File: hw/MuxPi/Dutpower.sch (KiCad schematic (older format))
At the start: 23 parts, among them P2 XY2500V-D(5.08)-2PIN, P3 XY2500V-D(5.08)-2PIN, Q1 2N7002, U15 MCP6002-E/SN, U4 ACS712ELCTR-05B-T

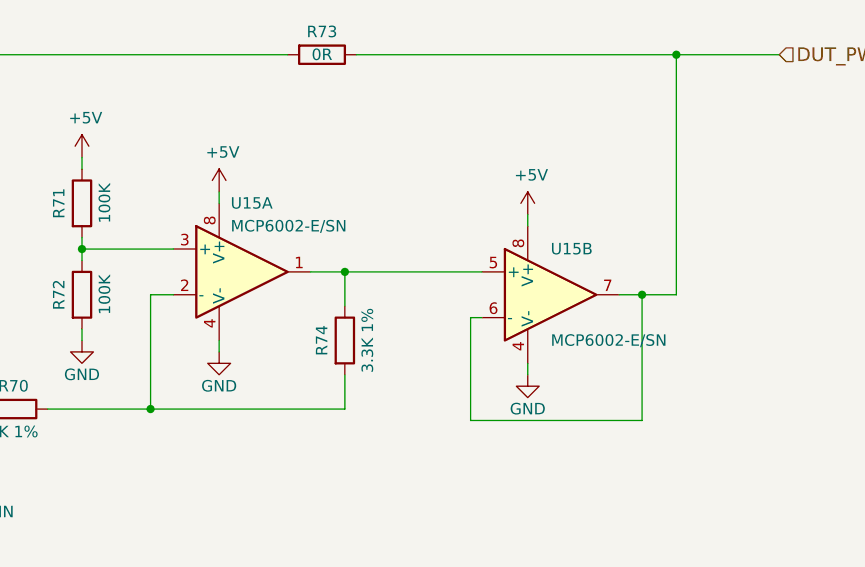
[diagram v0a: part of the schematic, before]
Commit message: Add detailed info to MuxPi electronic components
The additional information includes manufacturer names and
manufacturer symbols for all components except ceramic capacitors
and resistors. It allows to create BOM (Bill Of Materials) with
actual product names.

Change-Id: Id1c518bba60322d4b8b132ad14261806070abc27
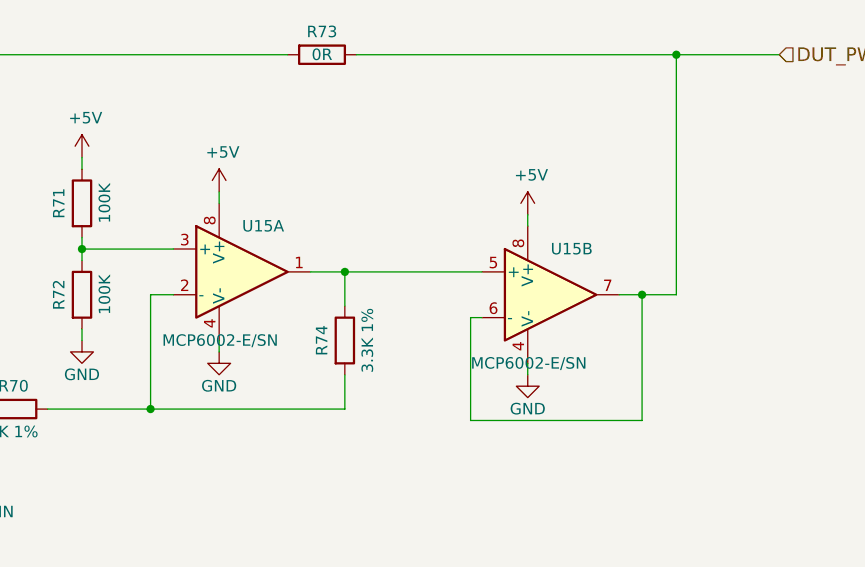
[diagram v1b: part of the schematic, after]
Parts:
- D1: Manufacturer (none) -> TAIWAN SEMICONDUCTOR; Symbol (none) -> ES1JL
- D12: Manufacturer (none) -> ON SEMICONDUCTOR (FAIRCHILD); Symbol (none) -> 1N4448WS
- P2, P3: Complementary manufacturer (none) -> XINYA; Complementary symbol (none) -> XY2500F-BV(5.08)-2P; Manufacturer (none) -> XINYA; Symbol (none) -> XY2500V-D(5.08)-2PIN
- Q1: Manufacturer (none) -> ON SEMICONDUCTOR (FAIRCHILD); Symbol (none) -> 2N7002
- RL1: Manufacturer (none) -> FUJITSU-TAKAMISAWA; Symbol (none) -> JV-5S-KT
- U15: Manufacturer (none) -> MICROCHIP TECHNOLOGY; Symbol (none) -> MCP6002-E/SN
- U4: Manufacturer (none) -> ALLEGRO MICROSYSTEMS; Symbol (none) -> ACS712ELCTR-05B-T
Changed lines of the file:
@@
 F 3 "http://www.tme.eu/pl/Document/6e3ed172b8ef57eec12ad172948b8283/ES1JL-DTE.pdf" H 3900 5000 60  0001 C CNN
 F 4 "http://www.tme.eu/pl/details/es1jl/diody-uniwersalne-smd/taiwan-semiconductor/" H 3900 5000 60  0001 C CNN "Shop link"
+F 5 "TAIWAN SEMICONDUCTOR" H 3900 5000 50  0001 C CNN "Manufacturer"
+F 6 "ES1JL" H 3900 5000 50  0001 C CNN "Symbol"
 	1    3900 5000
 	1    0    0    -1
@@
 F 3 "http://www.tme.eu/pl/Document/160416a7d37511bbe210dab3bc04735d/jv.pdf" H 3900 4400 50  0001 C CNN
 F 4 "http://www.tme.eu/pl/details/jv-5s-kt/przekazniki-elektromagn-miniaturowe/fujitsu-takamisawa/" V 3900 4400 60  0001 C CNN "Shop link"
+F 5 "FUJITSU-TAKAMISAWA" V 3900 4400 50  0001 C CNN "Manufacturer"
+F 6 "JV-5S-KT" V 3900 4400 50  0001 C CNN "Symbol"
 	1    3900 4400
 	0    -1   -1   0
@@
 F 4 "http://www.tme.eu/pl/details/tbg-5-pw-2p-gn/listwy-zaciskowe-do-druku/xinya/xy2500v-d508-2pin/" H 2300 3900 60  0001 C CNN "Shop link"
 F 5 "http://www.tme.eu/pl/details/tbw-5.08-2p/listwy-zaciskowe-do-druku/xinya/xy2500f-bv508-2p/" H 2300 3900 60  0001 C CNN "Complementary device"
+F 6 "XINYA" H 2300 3900 50  0001 C CNN "Complementary manufacturer"
+F 7 "XY2500F-BV(5.08)-2P" H 2300 3900 50  0001 C CNN "Complementary symbol"
+F 8 "XINYA" H 2300 3900 50  0001 C CNN "Manufacturer"
+F 9 "XY2500V-D(5.08)-2PIN" H 2300 3900 50  0001 C CNN "Symbol"
 	1    2300 3900
 	-1   0    0    -1
@@
 F 3 "http://www.farnell.com/datasheets/64754.pdf?_ga=1.192000233.291132730.1474618953" H 1690 1690 60  0001 C CNN
 F 4 "http://pl.farnell.com/allegro-microsystems/acs712elctr-05b-t/ic-sensor-current-5a-soic8/dp/1329623" V 3900 2800 60  0001 C CNN "Shop link"
+F 5 "ALLEGRO MICROSYSTEMS" V 3900 2800 50  0001 C CNN "Manufacturer"
+F 6 "ACS712ELCTR-05B-T " V 3900 2800 50  0001 C CNN "Symbol"
 	1    3900 2800
 	0    -1   -1   0
@@
 	0    1    1    0
 $EndComp
-$Comp
-L MuxPi:2N7002 Q1
-U 1 1 584F2EFF
-P 4200 5300
-F 0 "Q1" H 4391 5346 50  0000 L CNN
-F 1 "2N7002" H 4391 5255 50  0000 L CNN
-F 2 "TO_SOT_Packages_SMD:SOT-23" H 4400 5225 50  0001 L CIN
-F 3 "https://www.nxp.com/documents/data_sheet/2N7002.pdf" H 4200 5300 50  0001 L CNN
-F 4 "http://www.tme.eu/pl/details/2n7002/tranzystory-z-kanalem-n-smd/fairchild-semiconductor/" H 4200 5300 60  0001 C CNN "Shop link"
-	1    4200 5300
-	1    0    0    -1
-$EndComp
-$Comp
-L MuxPi:CONN_01X02 P3
-U 1 1 584FF008
-P 5950 3900
-F 0 "P3" H 6028 3941 50  0000 L CNN
-F 1 "XY2500V-D(5.08)-2PIN" H 6028 3850 50  0000 L CNN
-F 2 "mux-footprints:TerminalBlock_XY2500V-D(5.08)" H 5950 3900 50  0001 C CNN
-F 3 "http://www.cresttech.com.au/pdf/Pluggable_connector.pdf" H 5950 3900 50  0001 C CNN
-F 4 "http://www.tme.eu/pl/details/tbg-5-pw-2p-gn/listwy-zaciskowe-do-druku/xinya/xy2500v-d508-2pin/" H 5950 3900 60  0001 C CNN "Shop link"
-F 5 "http://www.tme.eu/pl/details/tbw-5.08-2p/listwy-zaciskowe-do-druku/xinya/xy2500f-bv508-2p/" H 5950 3900 60  0001 C CNN "Complementary device"
-	1    5950 3900
-	1    0    0    -1
-$EndComp
 Wire Wire Line
 	4600 3950 5050 3950
@@
 F 3 "https://www.tme.eu/pl/Document/092852c2250de492ce82b1b9e9d241c4/1N4148WS.pdf" H 5750 1950 50  0001 C CNN
 F 4 "https://www.tme.eu/pl/details/1n4448ws/diody-uniwersalne-smd/on-semiconductor-fairchild/" H 5750 1950 50  0001 C CNN "Shop link"
+F 5 "ON SEMICONDUCTOR (FAIRCHILD)" H 5750 1950 50  0001 C CNN "Manufacturer"
+F 6 "1N4448WS" H 5750 1950 50  0001 C CNN "Symbol"
 	1    5750 1950
 	-1   0    0    1
@@
 Wire Wire Line
 	5450 1950 5600 1950
-$Comp
-L MuxPi:MCP6002 U15
-U 1 1 5A9F2BE3
-P 7800 2900
-F 0 "U15" H 7750 3200 50  0000 L CNN
-F 1 "MCP6002-E/SN" H 7750 3100 50  0000 L CNN
-F 2 "mux-footprints:SOIC-8" H 7700 2950 50  0001 C CNN
-F 3 "http://www.tme.eu/pl/Document/c98656c49a036767b89c9bb93e3dda4a/mcp6001_2_4.pdf" H 7800 3050 50  0001 C CNN
-F 4 "http://www.tme.eu/pl/details/mcp6002-e_sn/wzmacniacze-operacyjne-smd/microchip-technology/" H 7800 2900 60  0001 C CNN "Shop link"
-	1    7800 2900
-	1    0    0    -1
-$EndComp
-$Comp
-L MuxPi:MCP6002 U15
-U 2 1 5A9F2BEB
-P 9150 3000
-F 0 "U15" H 9150 3200 50  0000 L CNN
-F 1 "MCP6002-E/SN" H 9150 2800 50  0000 L CNN
-F 2 "mux-footprints:SOIC-8" H 9050 3050 50  0001 C CNN
-F 3 "http://www.tme.eu/pl/Document/c98656c49a036767b89c9bb93e3dda4a/mcp6001_2_4.pdf" H 9150 3150 50  0001 C CNN
-F 4 "http://www.tme.eu/pl/details/mcp6002-e_sn/wzmacniacze-operacyjne-smd/microchip-technology/" H 9150 3000 60  0001 C CNN "Shop link"
-	2    9150 3000
-	1    0    0    -1
-$EndComp
 $Comp
 L MuxPi:GND #PWR0215
@@
 Wire Wire Line
 	6400 1950 8000 1950
+$Comp
+L MuxPi:2N7002 Q1
+U 1 1 5A8B550D
+P 4200 5300
+F 0 "Q1" H 4391 5346 50  0000 L CNN
+F 1 "2N7002" H 4391 5255 50  0000 L CNN
+F 2 "TO_SOT_Packages_SMD:SOT-23" H 4400 5225 50  0001 L CIN
+F 3 "https://www.nxp.com/documents/data_sheet/2N7002.pdf" H 4200 5300 50  0001 L CNN
+F 4 "http://www.tme.eu/pl/details/2n7002/tranzystory-z-kanalem-n-smd/fairchild-semiconductor/" H 4200 5300 60  0001 C CNN "Shop link"
+F 5 "ON SEMICONDUCTOR (FAIRCHILD)" H 4200 5300 50  0001 C CNN "Manufacturer"
+F 6 "2N7002" H 4200 5300 50  0001 C CNN "Symbol"
+	1    4200 5300
+	1    0    0    -1
+$EndComp
+$Comp
+L MuxPi:CONN_01X02 P3
+U 1 1 5A8B8B5B
+P 5950 3900
+F 0 "P3" H 6028 3941 50  0000 L CNN
+F 1 "XY2500V-D(5.08)-2PIN" H 6028 3850 50  0000 L CNN
+F 2 "mux-footprints:TerminalBlock_XY2500V-D(5.08)" H 5950 3900 50  0001 C CNN
+F 3 "http://www.cresttech.com.au/pdf/Pluggable_connector.pdf" H 5950 3900 50  0001 C CNN
+F 4 "http://www.tme.eu/pl/details/tbg-5-pw-2p-gn/listwy-zaciskowe-do-druku/xinya/xy2500v-d508-2pin/" H 5950 3900 60  0001 C CNN "Shop link"
+F 5 "http://www.tme.eu/pl/details/tbw-5.08-2p/listwy-zaciskowe-do-druku/xinya/xy2500f-bv508-2p/" H 5950 3900 60  0001 C CNN "Complementary device"
+F 6 "XINYA" H 5950 3900 50  0001 C CNN "Complementary manufacturer"
+F 7 "XY2500F-BV(5.08)-2P" H 5950 3900 50  0001 C CNN "Complementary symbol"
+F 8 "XINYA" H 5950 3900 50  0001 C CNN "Manufacturer"
+F 9 "XY2500V-D(5.08)-2PIN" H 5950 3900 50  0001 C CNN "Symbol"
+	1    5950 3900
+	1    0    0    -1
+$EndComp
+$Comp
+L MuxPi:MCP6002 U15
+U 1 1 5A8BCDE3
+P 7800 2900
+F 0 "U15" H 7800 3100 50  0000 L CNN
+F 1 "MCP6002-E/SN" H 7450 2600 50  0000 L CNN
+F 2 "mux-footprints:SOIC-8" H 7700 2950 50  0001 C CNN
+F 3 "http://www.tme.eu/pl/Document/c98656c49a036767b89c9bb93e3dda4a/mcp6001_2_4.pdf" H 7800 3050 50  0001 C CNN
+F 4 "http://www.tme.eu/pl/details/mcp6002-e_sn/wzmacniacze-operacyjne-smd/microchip-technology/" H 7800 2900 60  0001 C CNN "Shop link"
+F 5 "MICROCHIP TECHNOLOGY" H 7800 2900 50  0001 C CNN "Manufacturer"
+F 6 "MCP6002-E/SN" H 7800 2900 50  0001 C CNN "Symbol"
+	1    7800 2900
+	1    0    0    -1
+$EndComp
+$Comp
+L MuxPi:MCP6002 U15
+U 2 1 5A8BF6A4
+P 9150 3000
+F 0 "U15" H 9150 3200 50  0000 L CNN
+F 1 "MCP6002-E/SN" H 8800 2700 50  0000 L CNN
+F 2 "mux-footprints:SOIC-8" H 9050 3050 50  0001 C CNN
+F 3 "http://www.tme.eu/pl/Document/c98656c49a036767b89c9bb93e3dda4a/mcp6001_2_4.pdf" H 9150 3150 50  0001 C CNN
+F 4 "http://www.tme.eu/pl/details/mcp6002-e_sn/wzmacniacze-operacyjne-smd/microchip-technology/" H 9150 3000 60  0001 C CNN "Shop link"
+F 5 "MICROCHIP TECHNOLOGY" H 9150 3000 50  0001 C CNN "Manufacturer"
+F 6 "MCP6002-E/SN" H 9150 3000 50  0001 C CNN "Symbol"
+	2    9150 3000
+	1    0    0    -1
+$EndComp
 $EndSCHEMATC

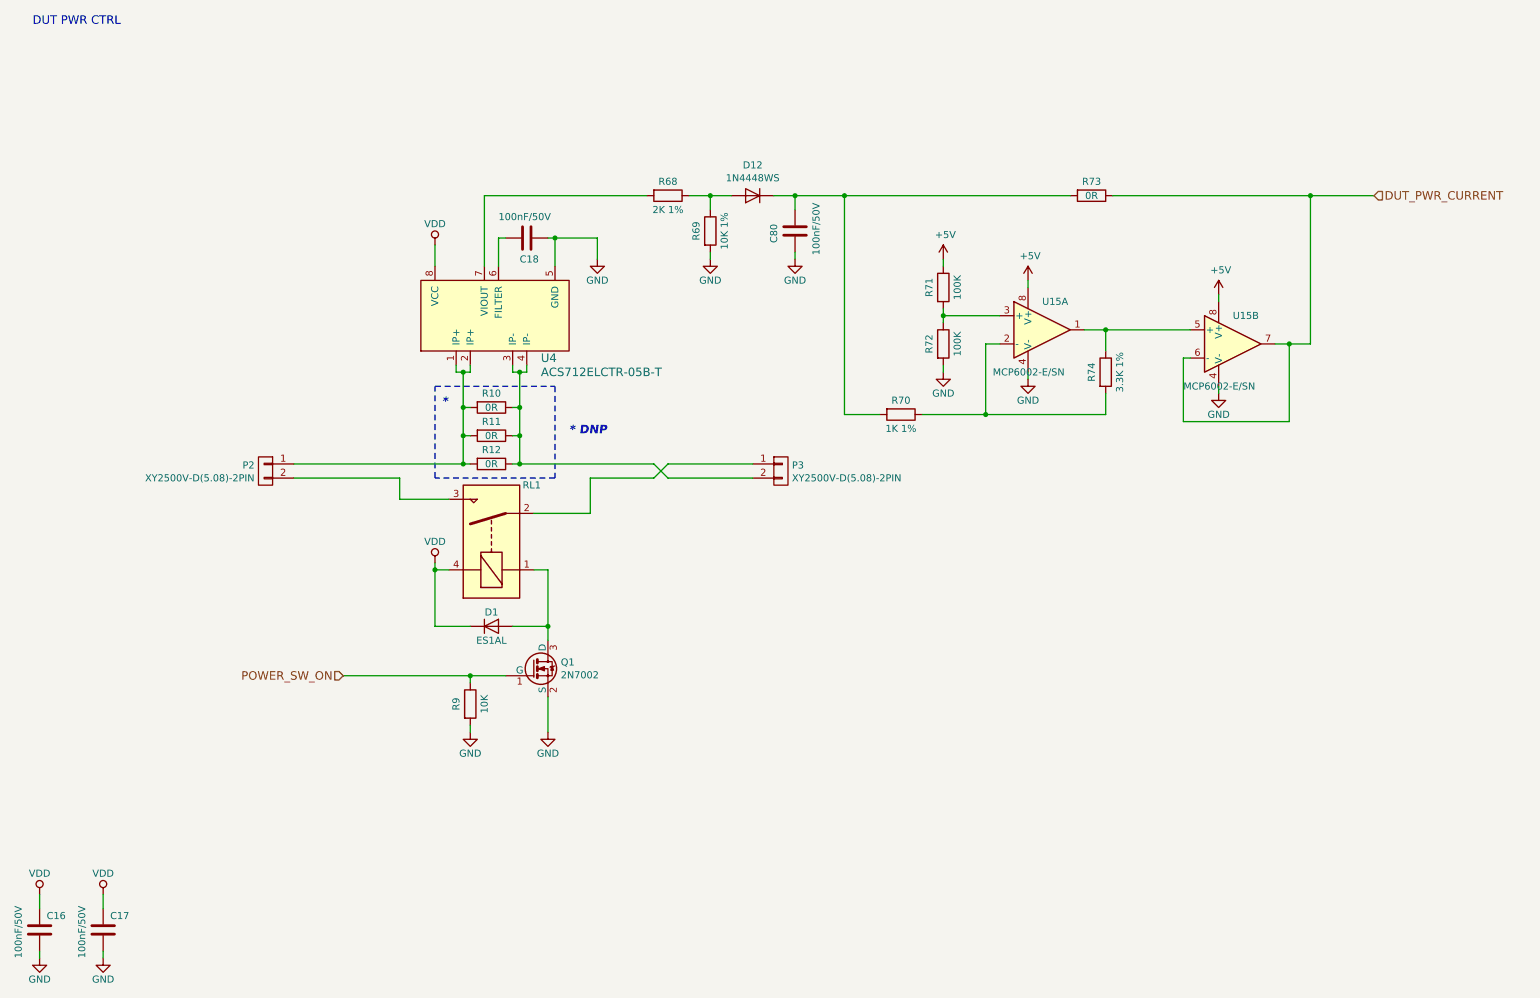
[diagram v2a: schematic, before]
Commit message: Update hardware design to version 1.2
Change-Id: I36445887bfaa5fada88d8bf3915603605de47512
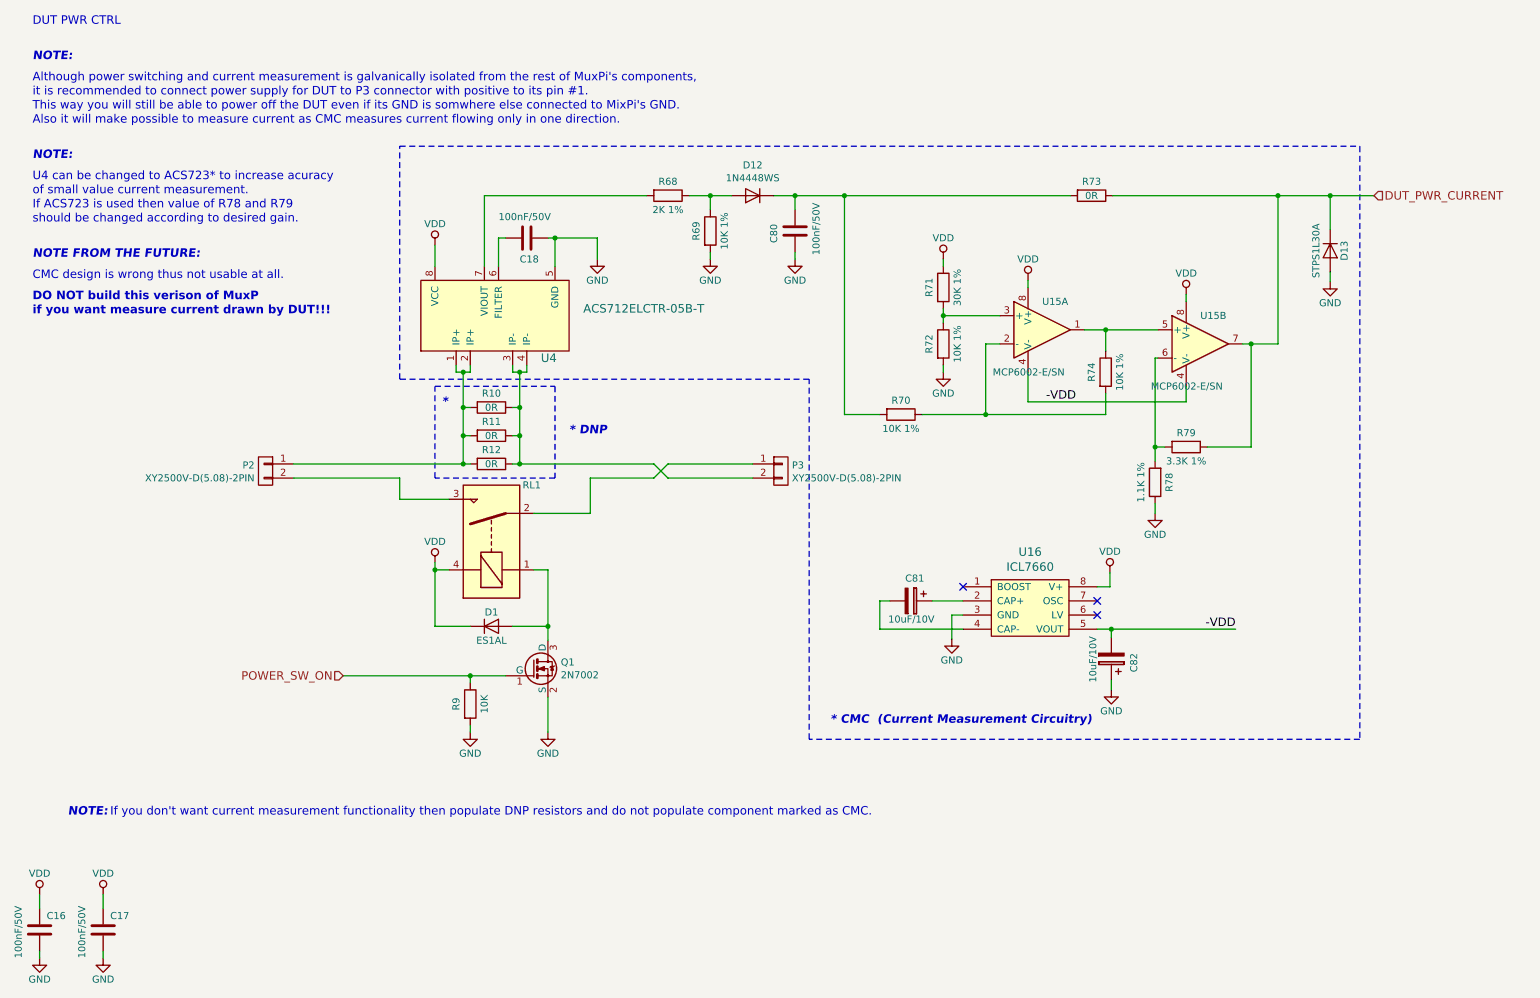
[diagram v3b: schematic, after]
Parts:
- added C81, C82: 10uF/10V, Capacitors_Tantalum_SMD:CP_Tantalum_Case-A_EIA-3216-18_Reflow, symbol MuxPi:CP
- added D13: STPS1L30A, mux-footprints:Sub_SMA, symbol MuxPi:D
- added R78: 1.1K 1%, Resistors_SMD:R_0805, symbol MuxPi:R
- added R79: 3.3K 1%, Resistors_SMD:R_0805, symbol MuxPi:R
- added U16: ICL7660, mux-footprints:SOIC-8, symbol MuxPi:ICL7660
- R70: value 1K 1% -> 10K 1%
- R71: value 100K -> 30K 1%
- R72: value 100K -> 10K 1%
- R74: value 3.3K 1% -> 10K 1%
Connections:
- net +5V is gone; now on net VDD: R71.1, U15.8 (V+), U15.8 (V+)
- net DUT_PWR_CURRENT: now also D13.1 (K), R79.1; no longer U15.6 (-)
- net GND: now also C82.1, D13.2 (A), R78.1, U16.3 (GND); no longer U15.4 (V-), U15.4 (V-)
- net VDD: now also U16.8 (V+)
- new net: R78.2, R79.2, U15.6 (-)
- new net: C81.1, U16.2 (CAP+)
- new net: C81.2, U16.4 (CAP-)
- new net -VDD: C82.2, U15.4 (V-), U15.4 (V-), U16.5 (VOUT)
- no-connect marks 0 -> 3
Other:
- note added: "* CMC (Current Measurement Circuitry)"
- note added: "Also it will make possible to measure current as CMC measures current flowing only in one direction."
- note added: "Although power switching and current measurement is galvanically isolated from the rest of MuxPi's components,"
- note added: "CMC design is wrong thus not usable at all.\n"
- note added: "DO NOT build this verison of MuxP"
- note added: "If ACS723 is used then value of R78 and R79"
- note added: "If you don't want current measurement functionality then populate DNP resistors and do not populate component marked as CMC."
- note added: "NOTE FROM THE FUTURE:\n"
- note added: "NOTE:"
- note added: "This way you will still be able to power off the DUT even if its GND is somwhere else connected to MixPi's GND."
- note added: "U4 can be changed to ACS723* to increase acuracy"
- note added: "if you want measure current drawn by DUT!!!"
- note added: "it is recommended to connect power supply for DUT to P3 connector with positive to its pin #1."
- note added: "of small value current measurement."
- note added: "should be changed according to desired gain."
- moved on the sheet: U15B

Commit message: Update hardware design to version 1.3
Change-Id: I17b3f32943a6fd048f05d1b0d8676607dc54b976
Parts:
- removed C80: 100nF/50V, Capacitors_SMD:C_0805, symbol MuxPi:C
- removed D12: 1N4448WS, Diodes_SMD:D_SOD-323F, symbol MuxPi:D
- removed R68: 2K 1%, Resistors_SMD:R_0805, symbol MuxPi:R
- removed R69: 10K 1%, Resistors_SMD:R_0805, symbol MuxPi:R
- removed R73: 0R, Resistors_SMD:R_0805, symbol MuxPi:R
- added RV2: POT, Potentiometers:Potentiometer_Trimmer_Bourns_3214J, symbol MuxPi:POT
- R72: value 10K 1% -> 8.2K 1%; Shop link http://www.tme.eu/pl/details/rc0805jr-07100k/rezystory-smd-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 -> https://www.tme.eu/pl/details/crcw08058k20fktabc/rezystory-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
- R78: value 1.1K 1% -> 1K 1%
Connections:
- net GND: now also U15.5 (+), RV2.3; no longer R72.2, R78.1
- net at U4.7 (VIOUT): now also R70.2
- net at R74.1, U15.1: now also R78.1; no longer U15.5 (+)
- new net: R72.2, RV2.2
- no-connect marks 3 -> 4
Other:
- note removed: "CMC design is wrong thus not usable at all.\n"
- note removed: "DO NOT build this verison of MuxP"
- note removed: "NOTE FROM THE FUTURE:\n"
- note removed: "if you want measure current drawn by DUT!!!"
- moved on the sheet: C18, C81, C82, D1, D13, P2, P3, Q1, R10, R11, R12, R70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

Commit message: Update  hardware design to version 1.4
Change-Id: I72a4381d8bec5616bc1cfe04dc8a5407141c77d5
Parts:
- removed C16, C17: 100nF/50V, Capacitors_SMD:C_0805, symbol MuxPi:C
- removed R79: 3.3K 1%, Resistors_SMD:R_0805, symbol MuxPi:R
- added RV3: 5k, MuxPi:Potentiometer_Trimmer_Bourns_3224W, symbol MuxPi:POT
- D13: footprint mux-footprints:Sub_SMA -> Diode_SMD:D_SMA
- RV2: value POT -> 5k; footprint Potentiometers:Potentiometer_Trimmer_Bourns_3214J -> MuxPi:Potentiometer_Trimmer_Bourns_3224W; Manufacturer (none) -> ALLCONNE; Shop link (none) -> https://www.maritex.com.pl/elementy_pasywne/potencjometry/w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; Symbol (none) -> 3224W-502-1LF
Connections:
- net DUT_PWR_CURRENT: now also RV3.3
- net at R78.2, U15.6 (-): now also RV3.2
- no-connect marks 4 -> 5
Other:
- note removed: "If ACS723 is used then value of R78 and R79"
- note removed: "should be changed according to desired gain."
- moved on the sheet: D13
